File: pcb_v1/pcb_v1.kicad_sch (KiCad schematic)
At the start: 8 parts, among them IC1 ESP32-WROOM-32UE-H4, IC2 DWM3000TR13, IC3 TC1017-3.3VLTTR, J1 Conn_02x03_Counter_Clockwise

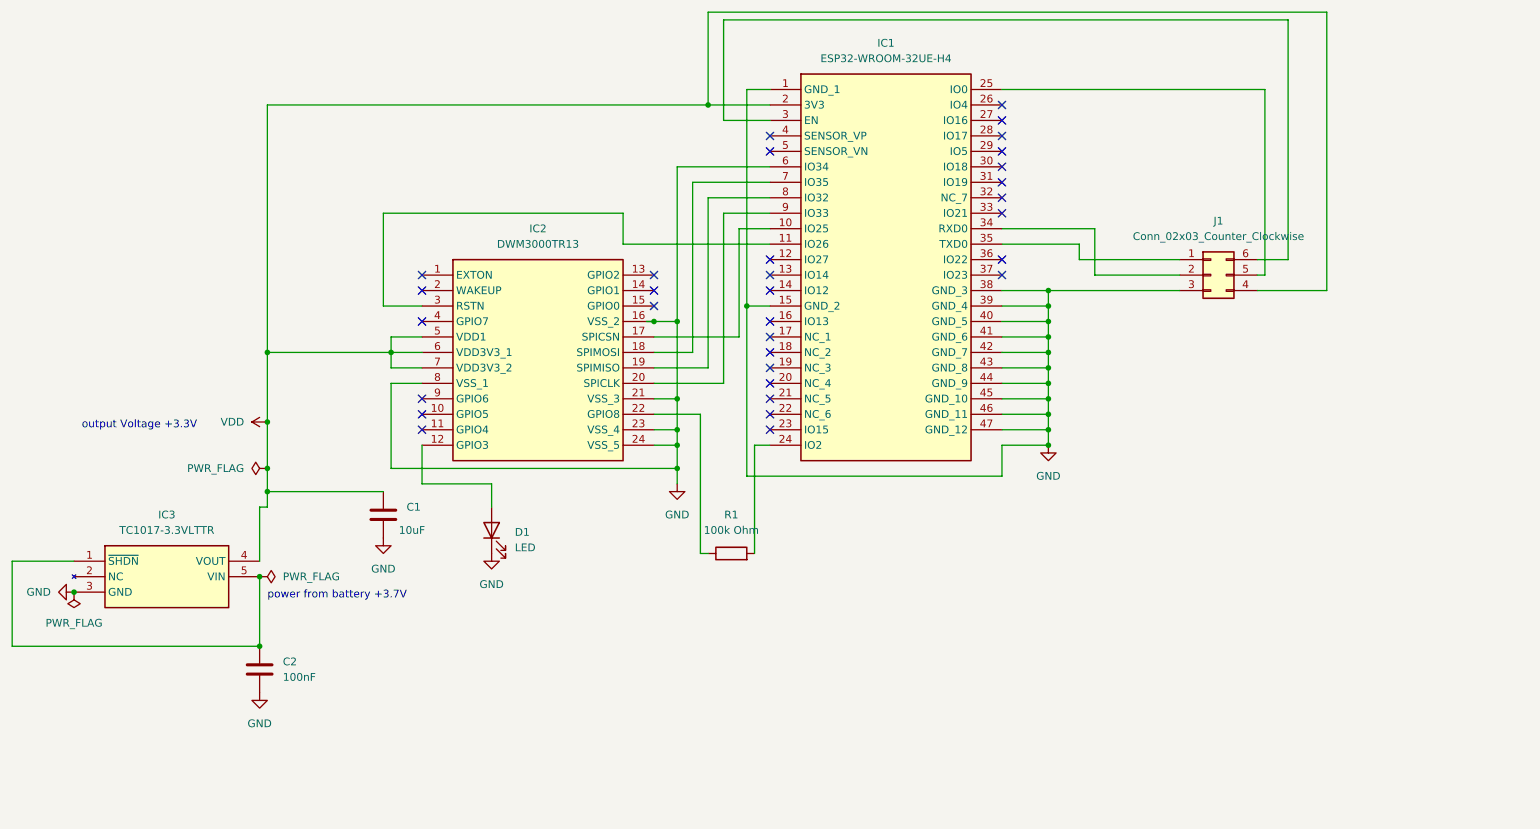
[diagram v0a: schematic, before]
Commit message: add schem files for capacitors and resistors, will be using smd componenets. added footprint assignments to pcb, so there will be changes there, but those footprint assignments are local. you must go to pcb editor, go to preferences and find foot print library manager, there you can assign footprints
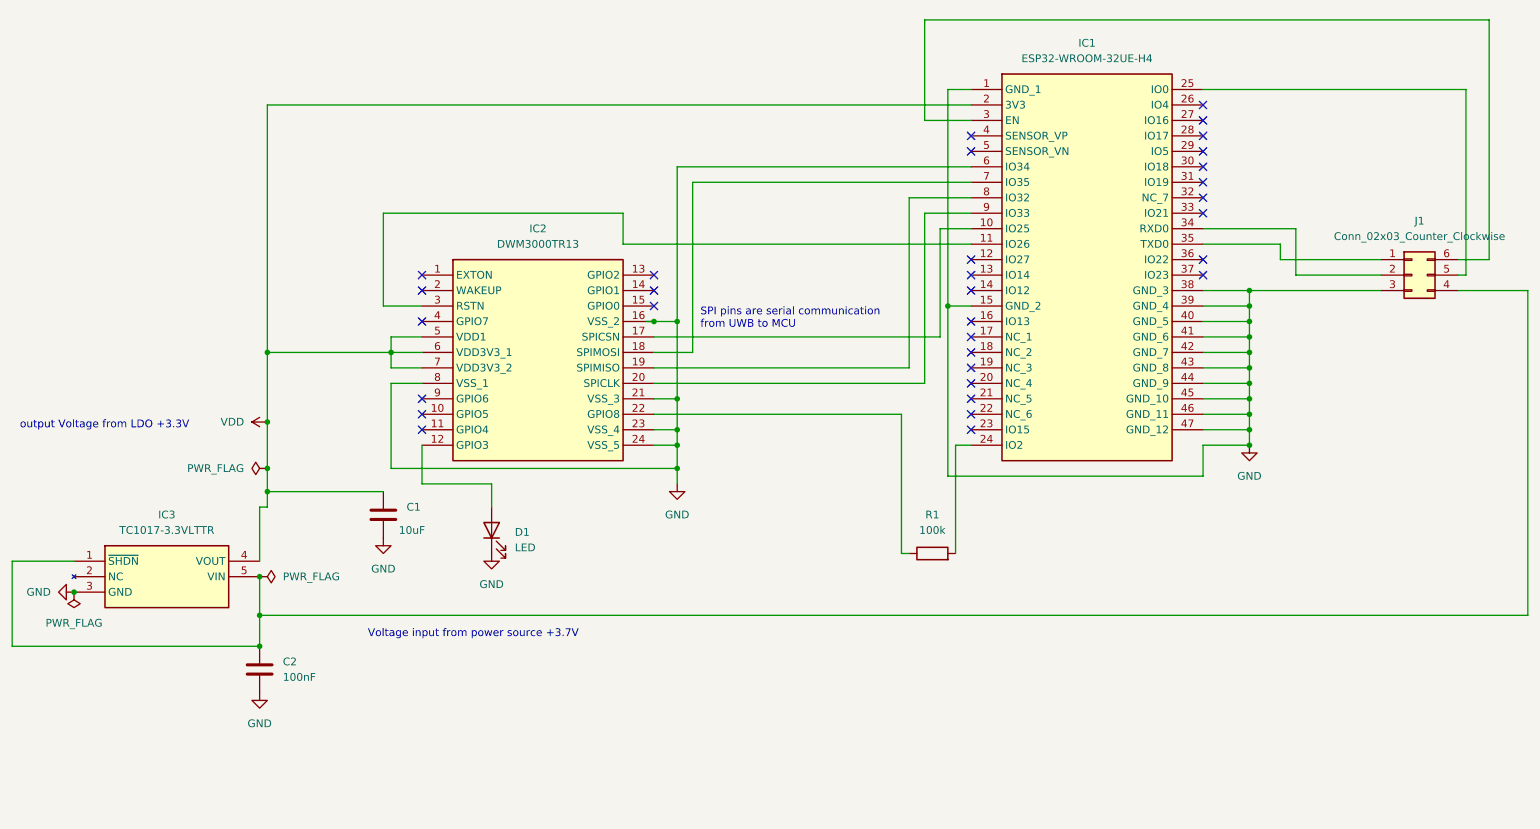
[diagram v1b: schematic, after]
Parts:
- IC1: footprint ESP32WROOM32UEH4 -> esp32_footprint:ESP32WROOM32UEH4
- IC2: footprint DWM3000TR13 -> dwm3000_footprint:XCVR_DWM3000TR13
- IC3: footprint SOT65P210X110-5N -> footprint:SOT65P210X110-5N
- J1: footprint Connector_IDC:IDC-Header_2x03_P2.54mm_Horizontal -> Connector_IDC:IDC-Header_2x03_P2.54mm_Vertical
- R1: value 100k Ohm -> 100k
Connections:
- net VDD: no longer J1.4 (Pin_4)
- net at C2.1, IC3.1 (~{SHDN}), IC3.5 (VIN): now also J1.4 (Pin_4)
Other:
- note added: "SPI pins are serial communication from UWB to MCU"
- note added: "Voltage input from power source +3.7V"
- note added: "output Voltage from LDO +3.3V"
- note removed: "output Voltage +3.3V"
- note removed: "power from battery +3.7V"
- moved on the sheet: IC1, J1, R1

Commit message: update pcb with current schematic, assigned footprints to caps and res, didn't wire anything
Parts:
- removed C1: 10uF, symbol Device:C
- removed C2: 100nF, symbol Device:C
- removed R1: 100k, symbol Device:R
- added C1: 100nF, 100nF_footprint:CAPC2012X94N, symbol KAM21BR71H104JT:KAM21BR71H104JT
- added C2: 10uF, 10uF_footprint:CAPC2012X140N, symbol GCM21BD70J106KE02L:GCM21BD70J106KE02L
- added R1, R2: 100k Ohm, 100kOhm_footprint:RESC5025X65N, symbol CRGP2010F100K:CRGP2010F100K
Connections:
- net GND: now also C1.2, C2.2
- net VDD: now also C2.1
- net at IC1.24 (IO2): now also R1.2
- net at IC2.12 (GPIO3): now also R2.1; no longer D1.2 (A)
- net at IC2.22 (GPIO8): now also R1.1
- net at IC3.1 (~{SHDN}), IC3.5 (VIN), J1.4 (Pin_4): now also C1.1
- new net: D1.2 (A), R2.2
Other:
- moved on the sheet: D1

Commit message: pcb edits. add led footprints
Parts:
- D1: footprint (none) -> led_footprint:QED123A4R0
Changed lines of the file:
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@@
       (effects (font (size 1.27 1.27)) (justify right))
     )
-    (property "Footprint" "" (at 115.57 135.89 0)
+    (property "Footprint" "led_footprint:QED123A4R0" (at 115.57 135.89 0)
       (effects (font (size 1.27 1.27)) hide)
     )

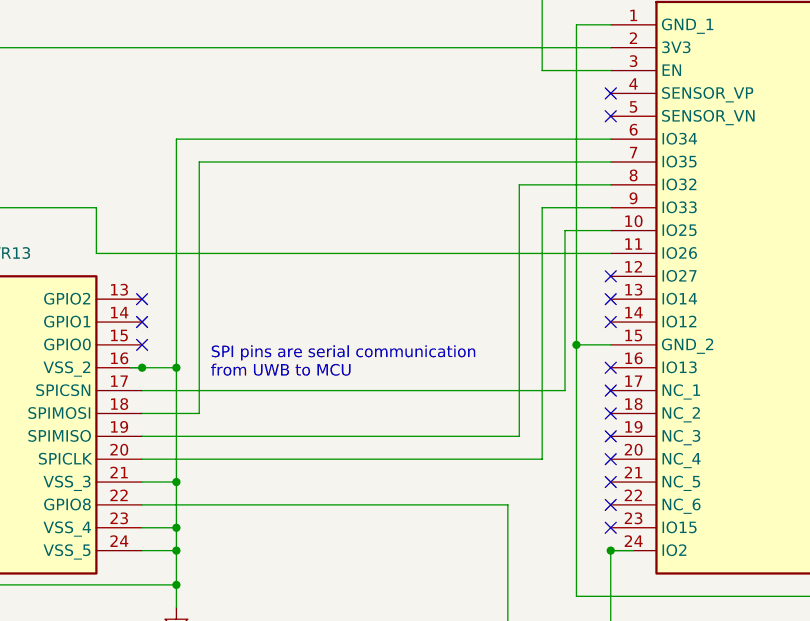
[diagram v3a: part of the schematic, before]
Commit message: update pin for jake baby
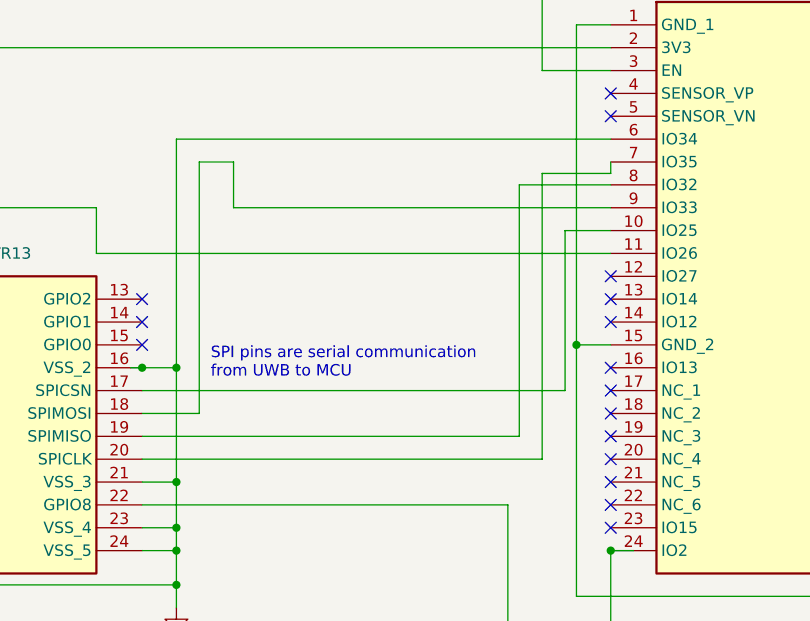
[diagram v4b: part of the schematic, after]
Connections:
- net at IC1.7 (IO35): now also IC2.20 (SPICLK); no longer IC2.18 (SPIMOSI)
- net at IC1.9 (IO33): now also IC2.18 (SPIMOSI); no longer IC2.20 (SPICLK)
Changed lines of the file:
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@@
+    (stroke (width 0) (type default))
+  )
+  (wire (pts (xy 140.97 82.55) (xy 182.88 82.55))
     (stroke (width 0) (type default))
   )
@@
     (stroke (width 0) (type default))
   )
+  (wire (pts (xy 140.97 77.47) (xy 140.97 82.55))
+    (stroke (width 0) (type default))
+  )
   (wire (pts (xy 220.98 95.25) (xy 228.6 95.25))
     (stroke (width 0) (type default))
@@
     (stroke (width 0) (type default))
   )
-  (wire (pts (xy 175.26 82.55) (xy 175.26 110.49))
+  (wire (pts (xy 175.26 78.74) (xy 175.26 110.49))
     (stroke (width 0) (type default))
   )
@@
     (stroke (width 0) (type default))
   )
+  (wire (pts (xy 175.26 78.74) (xy 182.88 78.74))
+    (stroke (width 0) (type default))
+  )
   (wire (pts (xy 67.31 128.27) (xy 86.36 128.27))
     (stroke (width 0) (type default))
@@
     (stroke (width 0) (type default))
   )
-  (wire (pts (xy 182.88 77.47) (xy 137.16 77.47))
-    (stroke (width 0) (type default))
-  )
   (wire (pts (xy 228.6 113.03) (xy 228.6 115.57))
     (stroke (width 0) (type default))
@@
     (stroke (width 0) (type default))
   )
-  (wire (pts (xy 182.88 82.55) (xy 175.26 82.55))
-    (stroke (width 0) (type default))
-  )
   (wire (pts (xy 130.81 100.33) (xy 134.62 100.33))
     (stroke (width 0) (type default))
@@
     (stroke (width 0) (type default))
   )
+  (wire (pts (xy 137.16 77.47) (xy 140.97 77.47))
+    (stroke (width 0) (type default))
+  )
   (wire (pts (xy 228.6 102.87) (xy 228.6 105.41))
     (stroke (width 0) (type default))
   )
+  (wire (pts (xy 182.88 78.74) (xy 182.88 77.47))
+    (stroke (width 0) (type default))
+  )

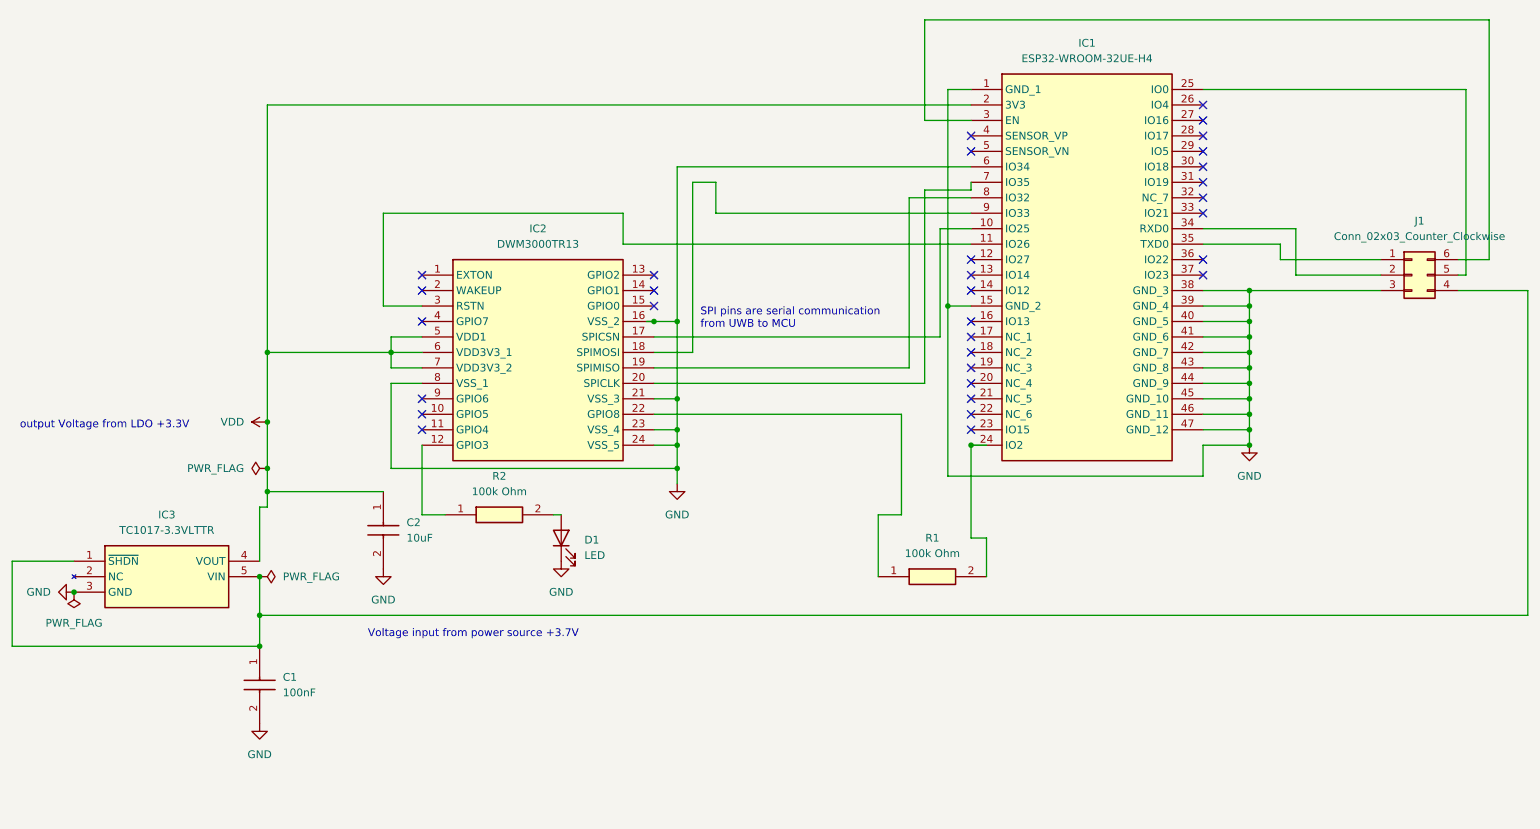
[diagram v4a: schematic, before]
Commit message: files for esp32 development. added li poly charger connector to schematic build.
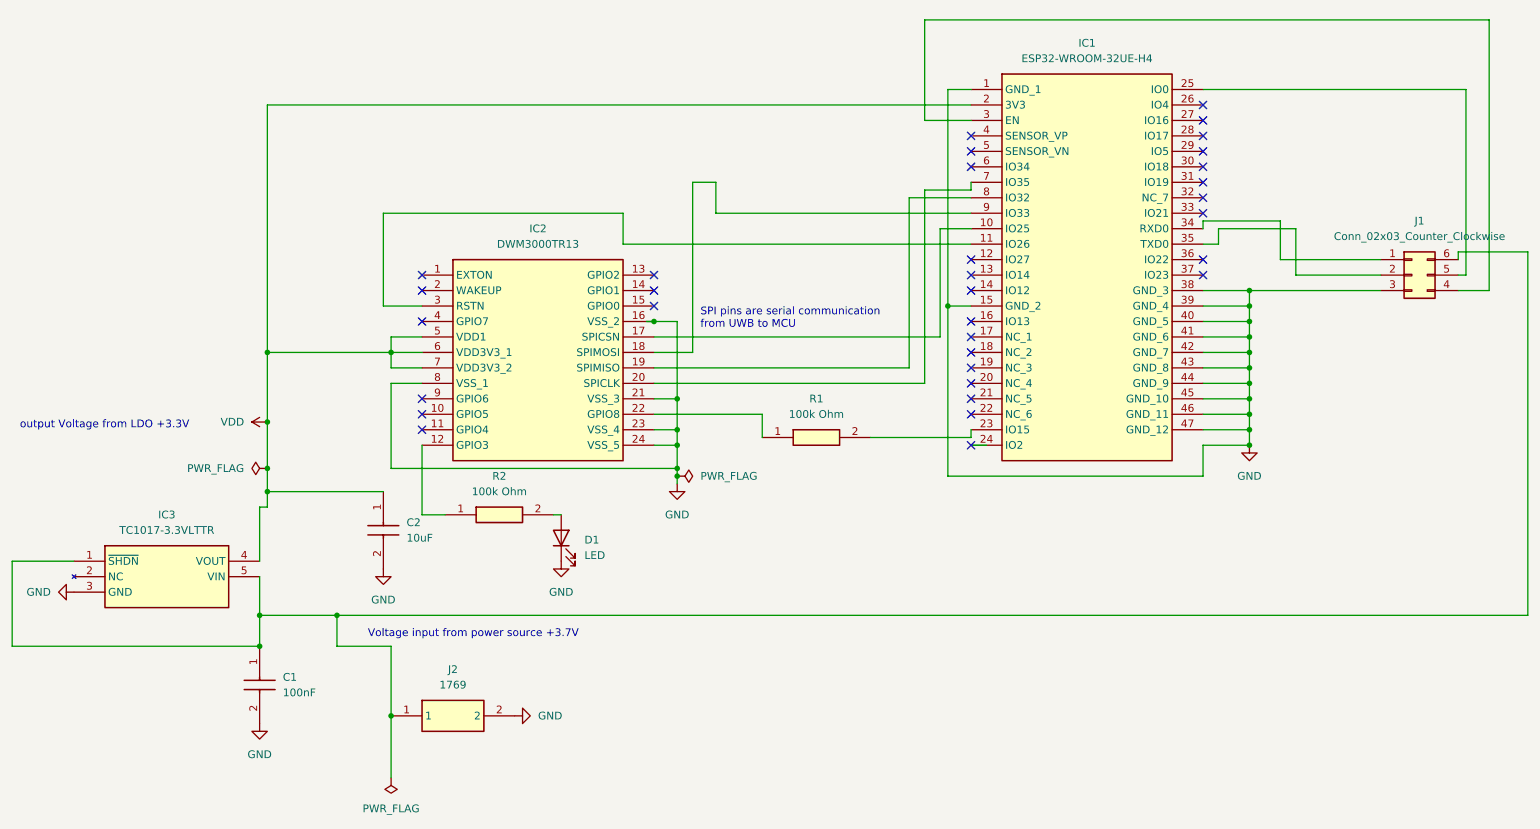
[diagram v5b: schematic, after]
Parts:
- added J2: 1769, lipo_charger_footprint:1769, symbol 1769:1769
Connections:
- net GND: now also J2.2; no longer IC1.6 (IO34)
- net at IC1.23 (IO15): now also R1.2
- net at IC1.24 (IO2): no longer R1.2
- net at IC1.3 (EN): now also J1.4 (Pin_4); no longer J1.6 (Pin_6)
- net at IC1.34 (RXD0): now also J1.1 (Pin_1); no longer J1.2 (Pin_2)
- net at IC1.35 (TXD0): now also J1.2 (Pin_2); no longer J1.1 (Pin_1)
- net at C1.1, IC3.1 (~{SHDN}), IC3.5 (VIN): now also J1.6 (Pin_6), J2.1; no longer J1.4 (Pin_4)
- no-connect marks 32 -> 33

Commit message: update pcb to use new mcu. the antennas are hanging off the pcb, and there are additional 1x4 pin headers for interfacing with unused GPIO pins just incase, and to flash code rx/tx.
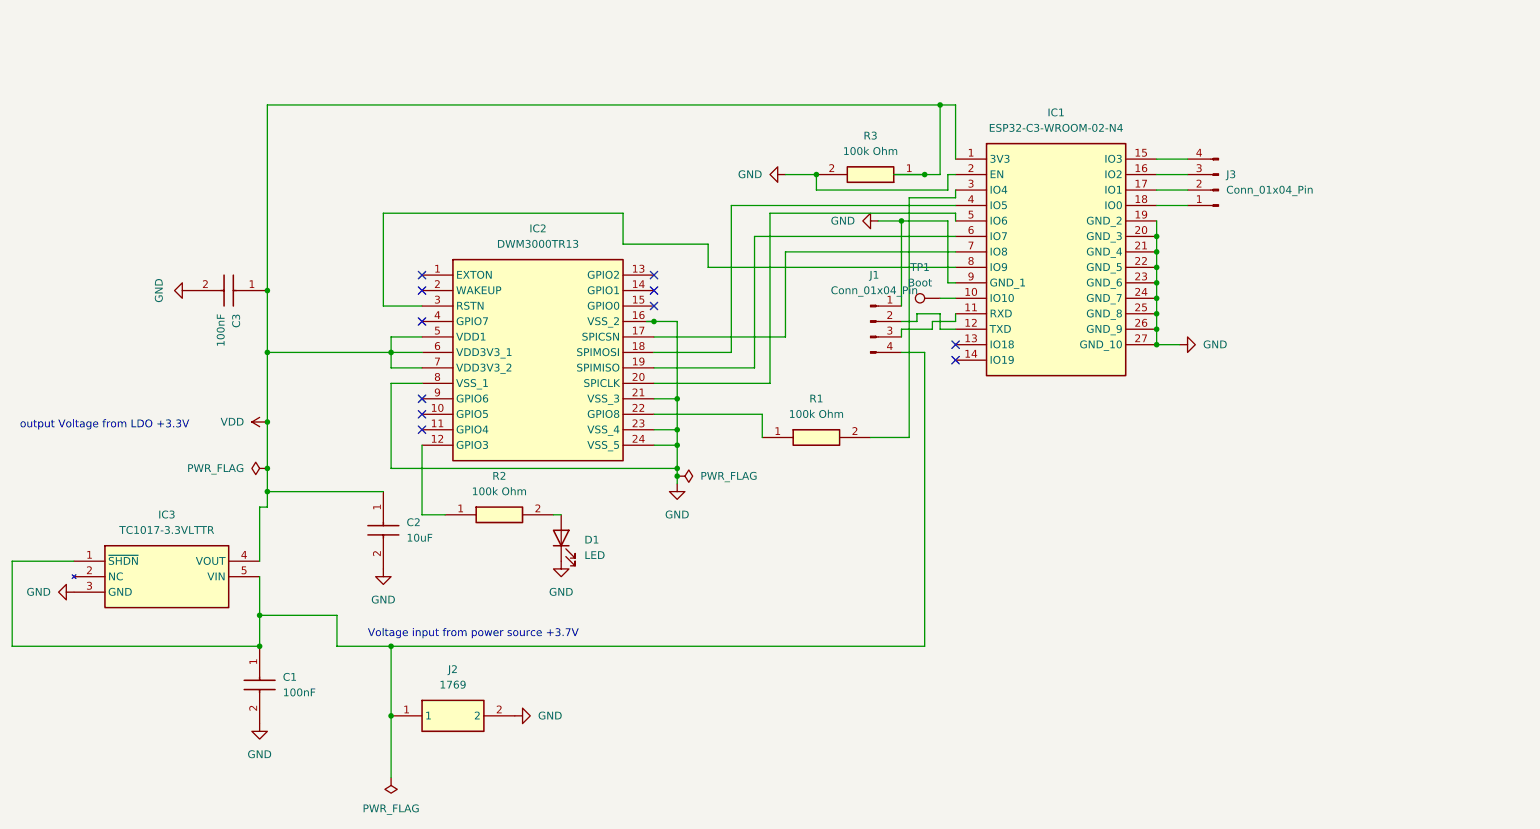
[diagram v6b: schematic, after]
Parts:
- removed IC1: ESP32-WROOM-32UE-H4, esp32_footprint:ESP32WROOM32UEH4, symbol ESP32-WROOM-32UE-H4:ESP32-WROOM-32UE-H4
- removed J1: Conn_02x03_Counter_Clockwise, Connector_IDC:IDC-Header_2x03_P2.54mm_Vertical, symbol Connector_Generic:Conn_02x03_Counter_Clockwise
- added C3: 100nF, 100nF_footprint:CAPC2012X94N, symbol KAM21BR71H104JT:KAM21BR71H104JT
- added IC1: ESP32-C3-WROOM-02-N4, esp_32_c3_footprint:ESP32C3WROOM02N4, symbol ESP32-C3-WROOM-02-N4:ESP32-C3-WROOM-02-N4
- added J1, J3: Conn_01x04_Pin, Connector_PinSocket_2.54mm:PinSocket_1x04_P2.54mm_Vertical, symbol Connector:Conn_01x04_Pin
- added R3: 100k Ohm, 100kOhm_footprint:RESC5025X65N, symbol CRGP2010F100K:CRGP2010F100K
- added TP1: Boot, Connector_PinSocket_2.54mm:PinSocket_1x01_P2.54mm_Vertical, symbol Connector:TestPoint
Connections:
- net GND: now also C3.2, IC1.19 (GND_2), IC1.2 (EN), IC1.20 (GND_3), IC1.21 (GND_4), IC1.22 (GND_5), IC1.23 (GND_6), IC1.24 (GND_7), IC1.25 (GND_8), IC1.26 (GND_9), IC1.27 (GND_10), IC1.9 (GND_1), J1.1 (Pin_1), R3.2
- net VDD: now also C3.1, IC1.1 (3V3), R3.1
- net at IC2.17 (SPICSN): now also IC1.7 (IO8)
- net at IC2.3 (RSTN): now also IC1.8 (IO9)
- net at R1.2: now also IC1.3 (IO4)
- net at IC2.20 (SPICLK): now also IC1.5 (IO6)
- net at IC2.19 (SPIMISO): now also IC1.6 (IO7)
- net at IC2.18 (SPIMOSI): now also IC1.4 (IO5)
- net at C1.1, IC3.1 (~{SHDN}), IC3.5 (VIN)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: now also J1.4 (Pin_4)
- new net: IC1.10 (IO10), TP1.1
- new net: IC1.11 (RXD), J1.3 (Pin_3)
- new net: IC1.12 (TXD), J1.2 (Pin_2)
- new net: IC1.15 (IO3), J3.4 (Pin_4)
- new net: IC1.16 (IO2), J3.3 (Pin_3)
- new net: IC1.17 (IO1), J3.2 (Pin_2)
- new net: IC1.18 (IO0), J3.1 (Pin_1)
- no-connect marks 33 -> 11
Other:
- note removed: "SPI pins are serial communication from UWB to MCU"
